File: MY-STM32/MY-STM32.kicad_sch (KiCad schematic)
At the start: 7 parts, among them U1 TLP250, U2 IH0515S

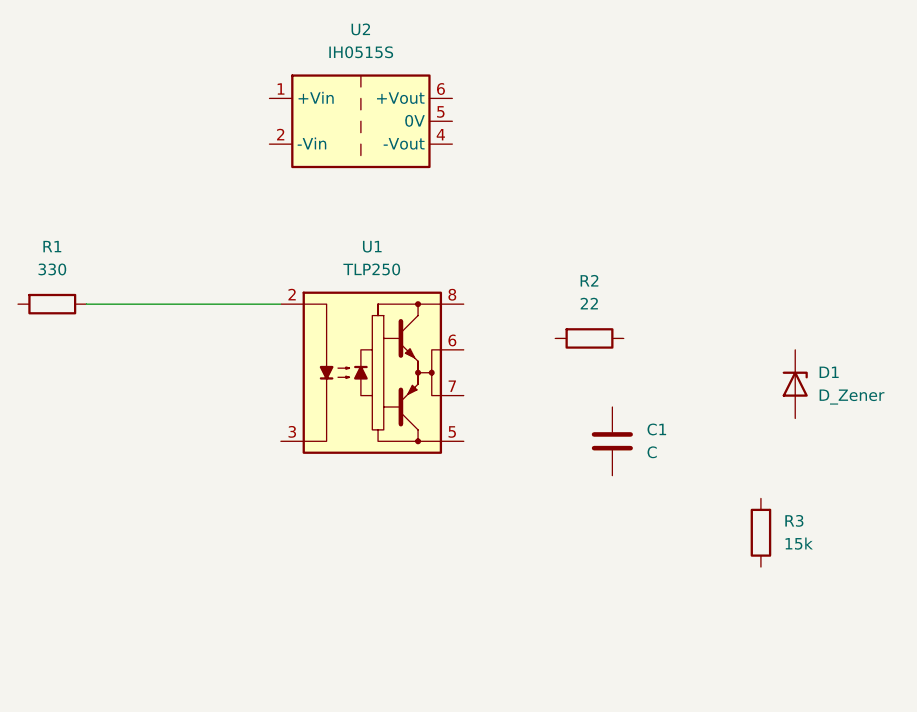
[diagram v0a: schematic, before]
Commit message: feat: add KiCad symbol parser and web preview
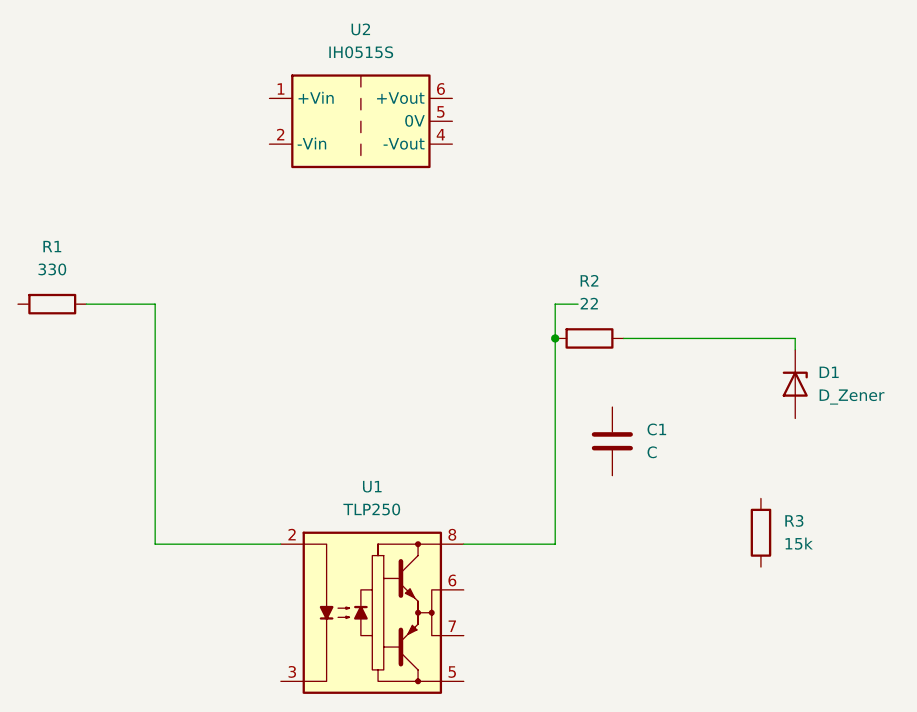
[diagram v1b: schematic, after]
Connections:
- net at U1.8 (VCC): now also R2.2
- net at R2.1: now also D1.1 (K)
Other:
- moved on the sheet: U1
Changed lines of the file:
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@@
 	(generator_version "10.0")
 	(paper "A4")
-	(wire
-		(pts
-			(xy 110.49 53.34) (xy 132.08 53.34)
+	(junction
+		(at 162.56 57.15)
+		(diameter 0)
+		(color 0 0 0 0)
+	)
+	(wire
+		(pts
+			(xy 170.18 57.15) (xy 189.23 57.15)
+		)
+		(stroke
+			(width 0)
+			(type default)
+		)
+	)
+	(wire
+		(pts
+			(xy 118.11 53.34) (xy 110.49 53.34)
+		)
+		(stroke
+			(width 0)
+			(type default)
+		)
+	)
+	(wire
+		(pts
+			(xy 162.56 80.01) (xy 162.56 57.15)
+		)
+		(stroke
+			(width 0)
+			(type default)
+		)
+	)
+	(wire
+		(pts
+			(xy 189.23 57.15) (xy 189.23 58.42)
+		)
+		(stroke
+			(width 0)
+			(type default)
+		)
+	)
+	(wire
+		(pts
+			(xy 162.56 53.34) (xy 165.1 53.34)
+		)
+		(stroke
+			(width 0)
+			(type default)
+		)
+	)
+	(wire
+		(pts
+			(xy 118.11 80.01) (xy 132.08 80.01)
+		)
+		(stroke
+			(width 0)
+			(type default)
+		)
+	)
+	(wire
+		(pts
+			(xy 152.4 80.01) (xy 162.56 80.01)
+		)
+		(stroke
+			(width 0)
+			(type default)
+		)
+	)
+	(wire
+		(pts
+			(xy 118.11 80.01) (xy 118.11 53.34)
+		)
+		(stroke
+			(width 0)
+			(type default)
+		)
+	)
+	(wire
+		(pts
+			(xy 162.56 53.34) (xy 162.56 57.15)
 		)
 		(stroke
@@
 	(symbol
 		(lib_id "Driver_FET:TLP250")
-		(at 142.24 60.96 0)
+		(at 142.24 87.63 0)
 		(unit 1)
 		(body_style 1)
@@
 		(fields_autoplaced yes)
 		(property "Reference" "U1"
-			(at 142.24 46.99 0)
+			(at 142.24 73.66 0)
 			(show_name no)
 			(do_not_autoplace no)
@@
 		)
 		(property "Value" "TLP250"
-			(at 142.24 49.53 0)
+			(at 142.24 76.2 0)
 			(show_name no)
 			(do_not_autoplace no)
@@
 		)
 		(property "Footprint" "Package_DIP:DIP-8_W7.62mm"
-			(at 142.24 71.12 0)
+			(at 142.24 97.79 0)
 			(hide yes)
 			(show_name no)
@@
 		)
 		(property "Datasheet" "http://toshiba.semicon-storage.com/info/docget.jsp?did=16821&prodName=TLP250"
-			(at 139.954 60.833 0)
+			(at 139.954 87.503 0)
 			(hide yes)
 			(show_name no)
@@
 		)
 		(property "Description" "Gate Drive Optocoupler, Output Current 1.5/1.5A, DIP-8"
-			(at 142.24 60.96 0)
-			(hide yes)
-			(show_name no)
+			(at 142.24 87.63 0)
+			(hide yes)
+			(show_name no)
